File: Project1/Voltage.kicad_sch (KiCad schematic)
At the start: 10 parts, among them U2 LM358

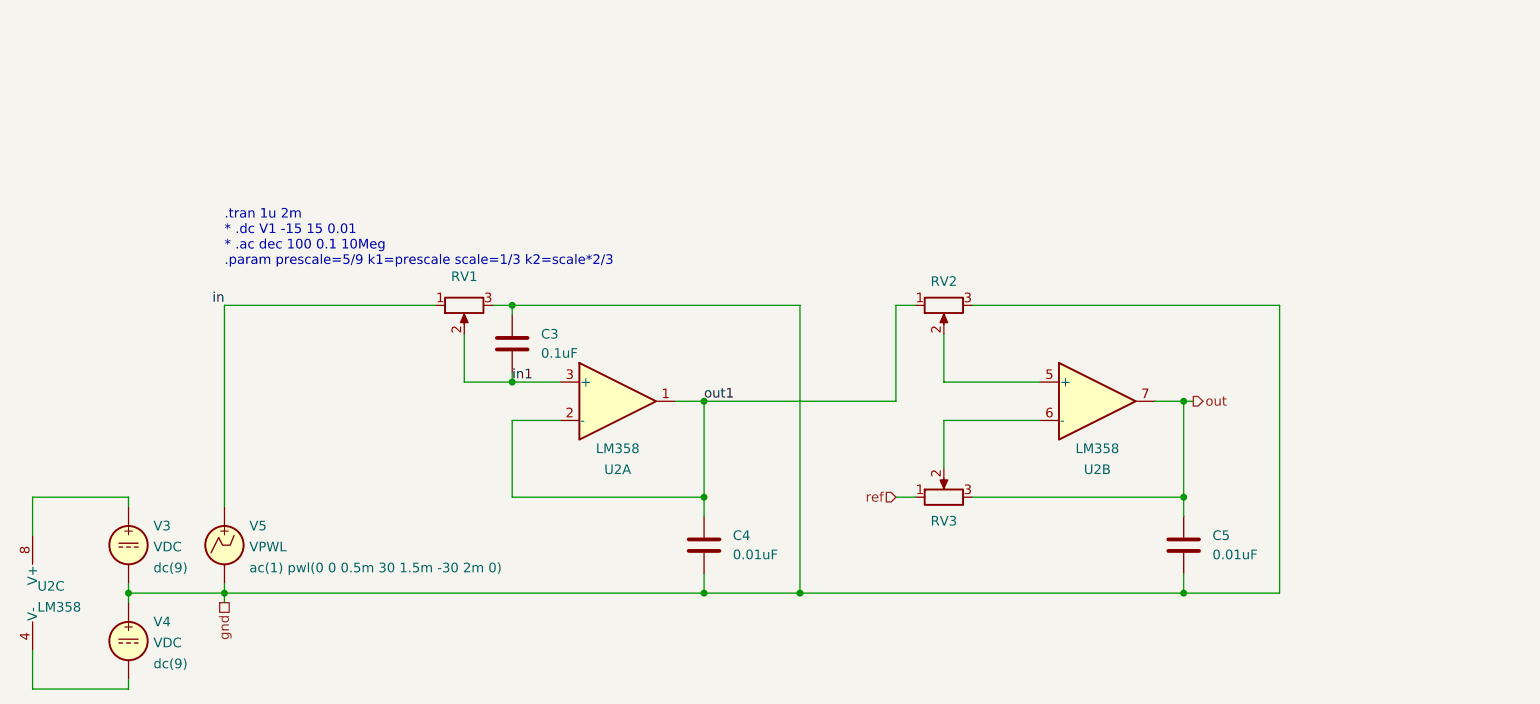
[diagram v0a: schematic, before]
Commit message: Updated voltage measurement
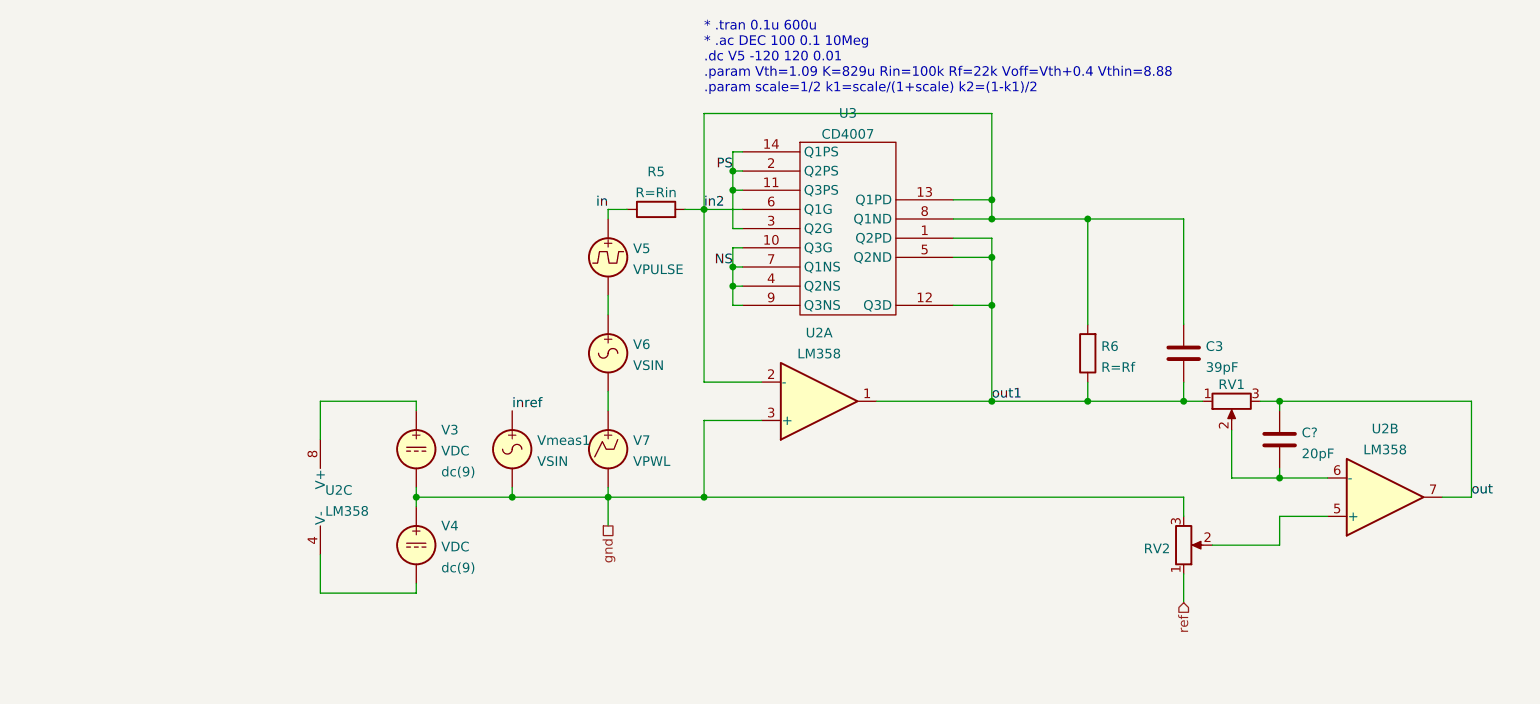
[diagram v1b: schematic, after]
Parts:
- removed C4, C5: 0.01uF, symbol Device:C
- removed RV3: R_Potentiometer, symbol Device:R_Potentiometer
- removed V5: VPWL, symbol Simulation_SPICE:VPWL
- added C?: 20pF, symbol Device:C
- added R5: R=Rin, symbol Device:R
- added R6: R=Rf, symbol Device:R
- added U3: CD4007, symbol Project1:CD4007
- added V5: VPULSE, symbol Simulation_SPICE:VPULSE
- added V6, Vmeas1: VSIN, symbol Simulation_SPICE:VSIN
- added V7: VPWL, symbol Simulation_SPICE:VPWL
- C3: value 0.1uF -> 39pF
- RV1: Spice_Model rpot k='k1' R=100k -> rpot k=k1 R=100k
- RV2: Spice_Model rpot k='k2' R=100k -> rpot k=k2 R=100k
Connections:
- net gnd: now also U2.3 (+), V7.2, Vmeas1.2; no longer C3.2, RV1.3
- net in: now also R5.1, V5.1; no longer RV1.1
- net out: now also RV1.3, C?.2
- net out1: now also C3.2, RV1.1, R6.1, U3.1 (Q2PD), U3.12 (Q3D), U3.5 (Q2ND); no longer RV2.1, U2.2 (-)
- net ref: now also RV2.1
- net at U2.6 (-): now also RV1.2, C?.1
- removed net in1: C3.1, RV1.2, U2.3 (+)
- new net: V6.2, V7.1
- new net: V5.2, V6.1
- new net NS: U3.10 (Q3G), U3.4 (Q2NS), U3.7 (Q1NS), U3.9 (Q3NS)
- new net PS: U3.11 (Q3PS), U3.14 (Q1PS), U3.2 (Q2PS), U3.3 (Q2G)
- new net in2: C3.1, R5.2, R6.2, U2.2 (-), U3.13 (Q1PD), U3.6 (Q1G), U3.8 (Q1ND)
- new net inref: Vmeas1.1
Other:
- note added: "* .tran 0.1u 600u * .ac DEC 100 0.1 10Meg .dc V5 -120 120 0.01 .param Vth=1.09 K=829u Rin=100k Rf=22k Voff=Vth+0.4 Vthin=8.88 .param scale=1/2 k1=scale/(1+scale) k2=(1-k1)/2"
- note removed: ".tran 1u 2m * .dc V1 -15 15 0.01 * .ac dec 100 0.1 10Meg .param prescale=5/9 k1=prescale scale=1/3 k2=scale*2/3"
- moved on the sheet: U2A, U2B, U2C, V3, V4

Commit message: Added switches, jumpers, and header
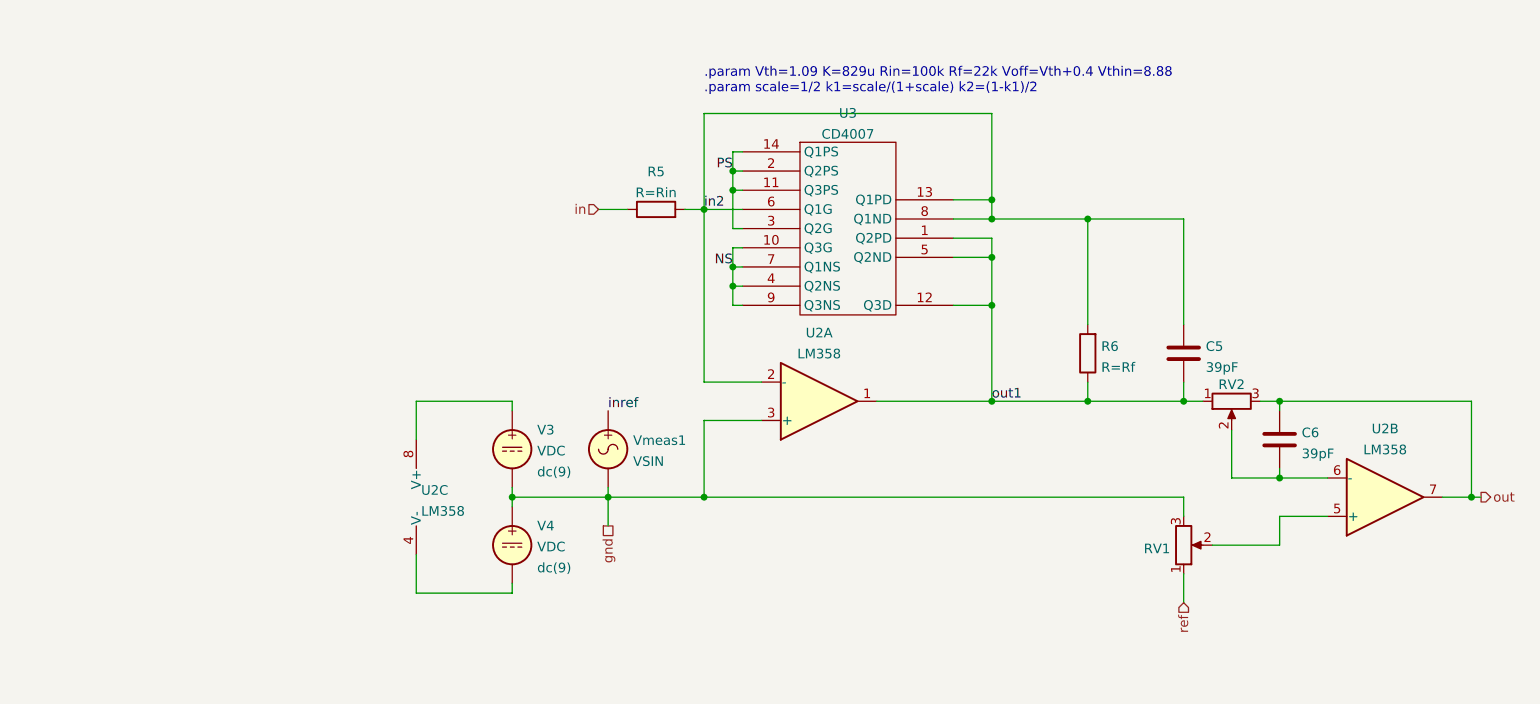
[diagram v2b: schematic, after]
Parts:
- removed V5: VPULSE, symbol Simulation_SPICE:VPULSE
- removed V6: VSIN, symbol Simulation_SPICE:VSIN
- removed V7: VPWL, symbol Simulation_SPICE:VPWL
- C6: renamed from C?; value 20pF -> 39pF
- renumbered C3 to C5, RV2 to RV1, RV1 to RV2
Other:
- note added: ".param Vth=1.09 K=829u Rin=100k Rf=22k Voff=Vth+0.4 Vthin=8.88 .param scale=1/2 k1=scale/(1+scale) k2=(1-k1)/2"
- note removed: "* .tran 0.1u 600u * .ac DEC 100 0.1 10Meg .dc V5 -120 120 0.01 .param Vth=1.09 K=829u Rin=100k Rf=22k Voff=Vth+0.4 Vthin=8.88 .param scale=1/2 k1=scale/(1+scale) k2=(1-k1)/2"
- moved on the sheet: U2C, V3, V4, Vmeas1

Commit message: Added protective diodes and centered circuit
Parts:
- renumbered V3 to V6, V4 to V7
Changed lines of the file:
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@@
   (symbol (lib_id "Simulation_SPICE:VDC") (at 114.3 107.95 0) (mirror y) (unit 1)
     (in_bom yes) (on_board yes) (fields_autoplaced)
-    (property "Reference" "V3" (id 0) (at 117.602 105.4046 0)
+    (property "Reference" "V6" (id 0) (at 117.602 105.4046 0)
       (effects (font (size 1.27 1.27)) (justify right))
     )
@@
   (symbol (lib_id "Simulation_SPICE:VDC") (at 114.3 120.65 0) (mirror y) (unit 1)
     (in_bom yes) (on_board yes) (fields_autoplaced)
-    (property "Reference" "V4" (id 0) (at 117.602 118.1046 0)
+    (property "Reference" "V7" (id 0) (at 117.602 118.1046 0)
       (effects (font (size 1.27 1.27)) (justify right))
     )

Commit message: Added headers for ADC and power
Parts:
- removed V6, V7: VDC, symbol Simulation_SPICE:VDC
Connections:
- net vcc: now reaches U2.8 (V+)
- net vee: now reaches U2.4 (V-)
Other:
- moved on the sheet: U2C
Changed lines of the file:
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@@
   (junction (at 241.3 114.3) (diameter 0) (color 0 0 0 0)
   )
-  (junction (at 114.3 114.3) (diameter 0) (color 0 0 0 0)
-  )
   (junction (at 215.9 101.6) (diameter 0) (color 0 0 0 0)
   )
@@
     (stroke (width 0) (type default) (color 0 0 0 0))
   )
-  (wire (pts (xy 101.6 127) (xy 114.3 127))
-    (stroke (width 0) (type default) (color 0 0 0 0))
-  )
   (wire (pts (xy 143.51 68.58) (xy 143.51 71.12))
     (stroke (width 0) (type default) (color 0 0 0 0))
   )
-  (wire (pts (xy 101.6 106.68) (xy 101.6 101.6))
+  (wire (pts (xy 114.3 100.33) (xy 114.3 106.68))
     (stroke (width 0) (type default) (color 0 0 0 0))
   )
@@
     (stroke (width 0) (type default) (color 0 0 0 0))
   )
-  (wire (pts (xy 114.3 114.3) (xy 114.3 115.57))
-    (stroke (width 0) (type default) (color 0 0 0 0))
-  )
-  (wire (pts (xy 127 114.3) (xy 114.3 114.3))
-    (stroke (width 0) (type default) (color 0 0 0 0))
-  )
-  (wire (pts (xy 114.3 127) (xy 114.3 125.73))
-    (stroke (width 0) (type default) (color 0 0 0 0))
-  )
   (wire (pts (xy 203.2 101.6) (xy 190.5 101.6))
     (stroke (width 0) (type default) (color 0 0 0 0))
@@
     (stroke (width 0) (type default) (color 0 0 0 0))
   )
-  (wire (pts (xy 101.6 121.92) (xy 101.6 127))
+  (wire (pts (xy 114.3 121.92) (xy 114.3 128.27))
     (stroke (width 0) (type default) (color 0 0 0 0))
   )
@@
     (stroke (width 0) (type solid) (color 0 0 0 0))
   )
-  (wire (pts (xy 114.3 102.87) (xy 114.3 101.6))
-    (stroke (width 0) (type default) (color 0 0 0 0))
-  )
   (wire (pts (xy 172.72 80.01) (xy 177.8 80.01))
     (stroke (width 0) (type default) (color 0 0 0 0))
@@
     (stroke (width 0) (type default) (color 0 0 0 0))
   )
-  (wire (pts (xy 101.6 101.6) (xy 114.3 101.6))
-    (stroke (width 0) (type default) (color 0 0 0 0))
-  )
   (wire (pts (xy 215.9 101.6) (xy 241.3 101.6))
     (stroke (width 0) (type default) (color 0 0 0 0))
@@
   )
   (wire (pts (xy 139.7 99.06) (xy 147.32 99.06))
-    (stroke (width 0) (type default) (color 0 0 0 0))
-  )
-  (wire (pts (xy 114.3 113.03) (xy 114.3 114.3))
     (stroke (width 0) (type default) (color 0 0 0 0))
   )
@@
     (effects (font (size 1.27 1.27)) (justify right))
   )
+  (hierarchical_label "vcc" (shape input) (at 114.3 100.33 90)
+    (effects (font (size 1.27 1.27)) (justify left))
+  )
   (hierarchical_label "in" (shape input) (at 125.73 76.2 180)
     (effects (font (size 1.27 1.27)) (justify right))
   )
   (hierarchical_label "gnd" (shape passive) (at 127 118.11 270)
+    (effects (font (size 1.27 1.27)) (justify right))
+  )
+  (hierarchical_label "vee" (shape input) (at 114.3 128.27 270)
     (effects (font (size 1.27 1.27)) (justify right))
   )
@@
     (pin "3")
   )
-  (symbol (lib_id "Simulation_SPICE:VDC") (at 114.3 107.95 0) (mirror y) (unit 1)
-    (in_bom yes) (on_board yes) (fields_autoplaced)
-    (property "Reference" "V6" (id 0) (at 117.602 105.4046 0)
-      (effects (font (size 1.27 1.27)) (justify right))
-    )
-    (property "Value" "VDC" (id 1) (at 117.602 108.1797 0)
-      (effects (font (size 1.27 1.27)) (justify right))
-    )
-    (property "Footprint" "" (id 2) (at 114.3 107.95 0)
-      (effects (font (size 1.27 1.27)) hide)
-    )
-    (property "Datasheet" "~" (id 3) (at 114.3 107.95 0)
-      (effects (font (size 1.27 1.27)) hide)
-    )
-    (property "Spice_Netlist_Enabled" "Y" (id 4) (at 114.3 107.95 0)
-      (effects (font (size 1.27 1.27)) (justify left) hide)
-    )
-    (property "Spice_Primitive" "V" (id 5) (at 114.3 107.95 0)
-      (effects (font (size 1.27 1.27)) (justify left) hide)
-    )
-    (property "Spice_Model" "dc(9)" (id 6) (at 117.602 110.9548 0)
-      (effects (font (size 1.27 1.27)) (justify right))
-    )
-    (pin "1")
-    (pin "2")
-  )
-  (symbol (lib_id "Simulation_SPICE:VDC") (at 114.3 120.65 0) (mirror y) (unit 1)
-    (in_bom yes) (on_board yes) (fields_autoplaced)
-    (property "Reference" "V7" (id 0) (at 117.602 118.1046 0)
-      (effects (font (size 1.27 1.27)) (justify right))
-    )
-    (property "Value" "VDC" (id 1) (at 117.602 120.8797 0)
-      (effects (font (size 1.27 1.27)) (justify right))
-    )
-    (property "Footprint" "" (id 2) (at 114.3 120.65 0)
-      (effects (font (size 1.27 1.27)) hide)
-    )
-    (property "Datasheet" "~" (id 3) (at 114.3 120.65 0)
-      (effects (font (size 1.27 1.27)) hide)
-    )
-    (property "Spice_Netlist_Enabled" "Y" (id 4) (at 114.3 120.65 0)
-      (effects (font (size 1.27 1.27)) (justify left) hide)
-    )
-    (property "Spice_Primitive" "V" (id 5) (at 114.3 120.65 0)
-      (effects (font (size 1.27 1.27)) (justify left) hide)
-    )
-    (property "Spice_Model" "dc(9)" (id 6) (at 117.602 123.6548 0)
-      (effects (font (size 1.27 1.27)) (justify right))
-    )
-    (pin "1")
-    (pin "2")
-  )
   (symbol (lib_id "Amplifier_Operational:LM358") (at 229.87 114.3 0) (mirror x) (unit 2)
     (in_bom yes) (on_board yes) (fields_autoplaced)
@@
     (pin "7")
   )
-  (symbol (lib_id "Amplifier_Operational:LM358") (at 104.14 114.3 0) (unit 3)
-    (in_bom yes) (on_board yes) (fields_autoplaced)
-    (property "Reference" "U2" (id 0) (at 102.235 113.3915 0)
+  (symbol (lib_id "Amplifier_Operational:LM358") (at 116.84 114.3 0) (unit 3)
+    (in_bom yes) (on_board yes) (fields_autoplaced)
+    (property "Reference" "U2" (id 0) (at 114.935 113.3915 0)
       (effects (font (size 1.27 1.27)) (justify left))
     )
-    (property "Value" "LM358" (id 1) (at 102.235 116.1666 0)
+    (property "Value" "LM358" (id 1) (at 114.935 116.1666 0)
       (effects (font (size 1.27 1.27)) (justify left))
     )
-    (property "Footprint" "" (id 2) (at 104.14 114.3 0)
-      (effects (font (size 1.27 1.27)) hide)
-    )
-    (property "Datasheet" "http://www.ti.com/lit/ds/symlink/lm2904-n.pdf" (id 3) (at 104.14 114.3 0)
-      (effects (font (size 1.27 1.27)) hide)
-    )
-    (property "Spice_Primitive" "X" (id 4) (at 104.14 114.3 0)
-      (effects (font (size 1.27 1.27)) hide)
-    )
-    (property "Spice_Model" "lm358" (id 5) (at 104.14 114.3 0)
-      (effects (font (size 1.27 1.27)) hide)
-    )
-    (property "Spice_Netlist_Enabled" "Y" (id 6) (at 104.14 114.3 0)
-      (effects (font (size 1.27 1.27)) hide)
-    )
-    (property "Spice_Lib_File" "SPICE.lib" (id 7) (at 104.14 114.3 0)
-      (effects (font (size 1.27 1.27)) hide)
-    )
+    (property "Footprint" "" (id 2) (at 116.84 114.3 0)
+      (effects (font (size 1.27 1.27)) hide)
+    )
+    (property "Datasheet" "http://www.ti.com/lit/ds/symlink/lm2904-n.pdf" (id 3) (at 116.84 114.3 0)
+      (effects (font (size 1.27 1.27)) hide)
+    )
+    (property "Spice_Primitive" "X" (id 4) (at 116.84 114.3 0)
+      (effects (font (size 1.27 1.27)) hide)
+    )
+    (property "Spice_Model" "lm358" (id 5) (at 116.84 114.3 0)
+      (effects (font (size 1.27 1.27)) hide)
+    )
+    (property "Spice_Netlist_Enabled" "Y" (id 6) (at 116.84 114.3 0)
+      (effects (font (size 1.27 1.27)) hide)
+    )
+    (property "Spice_Lib_File" "SPICE.lib" (id 7) (at 116.84 114.3 0)
+      (effects (font (size 1.27 1.27)) hide)
+    )
